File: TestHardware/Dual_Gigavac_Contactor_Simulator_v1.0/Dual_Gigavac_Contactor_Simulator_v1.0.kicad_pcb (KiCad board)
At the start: 2 copper layers, 48.1 x 35.4 mm, 69 parts, among them J1 Signal, J2 Power, J3 Contactor Driver 1, J4 Contactor Sense 2, J5 Contactor Sense 1, J6 Contactor Driver 2, Q1 Q_NMOS_DUAL_SGD, Q2 Q_NMOS_DUAL_SGD, Q3 Q_NMOS_DUAL_SGD, SW1 SW_Push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

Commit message: Minor tweaks
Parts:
- moved R22 0.13 mm to (137.5, 104.8)
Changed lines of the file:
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@@
   )
   (module Resistor_SMD:R_0603_1608Metric_Pad1.05x0.95mm_HandSolder (layer B.Cu)
-    (at 137.525 104.675)
+    (at 137.5 104.8)
     (descr "Resistor SMD 0603 (1608 Metric), square (rectangular) end terminal, IPC_7351 nominal with elongated pad for handsoldering. (Body size source: http://www.tortai-tech.com/upload/download/2011102023233369053.pdf), generated with kicad-footprint-generator")
     (tags "resistor handsolder")
@@
   (segment (start 120.25 112) (end 120.55 112.3) (width 0.2) (layer B.Cu) (net 25))
   (segment (start 121.025 112.775) (end 120.55 112.3) (width 0.2) (layer B.Cu) (net 25))
-  (via (at 120.125 104.3) (size 0.7) (drill 0.3) (layers F.Cu B.Cu) (net 26))
-  (segment (start 120.125 105.5) (end 120.125 104.3) (width 0.2) (layer B.Cu) (net 26))
-  (segment (start 120.125 104.3) (end 120.125 105.5) (width 0.2) (layer F.Cu) (net 26))
+  (segment (start 120.125 104.319254) (end 120.13569 104.308564) (width 0.2) (layer B.Cu) (net 26))
+  (segment (start 120.125 105.5) (end 120.125 104.319254) (width 0.2) (layer F.Cu) (net 26))
+  (segment (start 120.125 105.5) (end 120.125 104.319254) (width 0.2) (layer B.Cu) (net 26))
+  (segment (start 120.125 104.319254) (end 120.13569 104.308564) (width 0.2) (layer F.Cu) (net 26))
+  (via (at 120.13569 104.308564) (size 0.7) (drill 0.3) (layers F.Cu B.Cu) (net 26))
   (via (at 127.275 104.225) (size 0.7) (drill 0.3) (layers F.Cu B.Cu) (net 27))
   (segment (start 127.275 105.5) (end 127.275 104.225) (width 0.2) (layer B.Cu) (net 27))
@@
   (segment (start 130.025 114.575) (end 130.374999 114.225001) (width 0.2) (layer B.Cu) (net 37))
   (segment (start 130.374999 114.225001) (end 130.749999 114.225001) (width 0.2) (layer B.Cu) (net 37))
-  (segment (start 133.975 111.8) (end 132.9 111.8) (width 0.2) (layer F.Cu) (net 37))
-  (segment (start 135.8 109.975) (end 133.975 111.8) (width 0.2) (layer F.Cu) (net 37))
-  (segment (start 135.8 109.26) (end 135.8 109.975) (width 0.2) (layer F.Cu) (net 37))
+  (segment (start 133.025 111.8) (end 132.9 111.8) (width 0.2) (layer F.Cu) (net 37))
+  (segment (start 133.05 111.825) (end 133.025 111.8) (width 0.2) (layer F.Cu) (net 37))
+  (segment (start 133.235 111.825) (end 133.05 111.825) (width 0.2) (layer F.Cu) (net 37))
   (segment (start 138.4 107.86) (end 137.2 107.86) (width 0.2) (layer F.Cu) (net 37))
-  (segment (start 137.2 107.86) (end 135.8 109.26) (width 0.2) (layer F.Cu) (net 37))
+  (segment (start 137.2 107.86) (end 133.235 111.825) (width 0.2) (layer F.Cu) (net 37))
   (segment (start 122.45 110.675) (end 122.475 110.65) (width 0.2) (layer B.Cu) (net 38))
   (segment (start 122.45 113.425) (end 122.45 110.675) (width 0.2) (layer B.Cu) (net 38))
@@
   (segment (start 120.575 109.35) (end 121.1 109.35) (width 0.2) (layer B.Cu) (net 38))
   (segment (start 121.1 109.35) (end 121.3 109.55) (width 0.2) (layer B.Cu) (net 38))
-  (segment (start 120 100) (end 120 103.15) (width 0.2) (layer F.Cu) (net 38))
-  (segment (start 118.799999 104.725001) (end 118.05 105.475) (width 0.2) (layer F.Cu) (net 38))
-  (segment (start 118.799999 104.350001) (end 118.799999 104.725001) (width 0.2) (layer F.Cu) (net 38))
-  (segment (start 120 103.15) (end 118.799999 104.350001) (width 0.2) (layer F.Cu) (net 38))
+  (segment (start 120 103.525) (end 118.05 105.475) (width 0.2) (layer F.Cu) (net 38))
+  (segment (start 120 100) (end 120 103.525) (width 0.2) (layer F.Cu) (net 38))
   (zone (net 10) (net_name +3V3) (layer F.Cu) (hatch edge 0.508)
     (connect_pads (clearance 0.508))

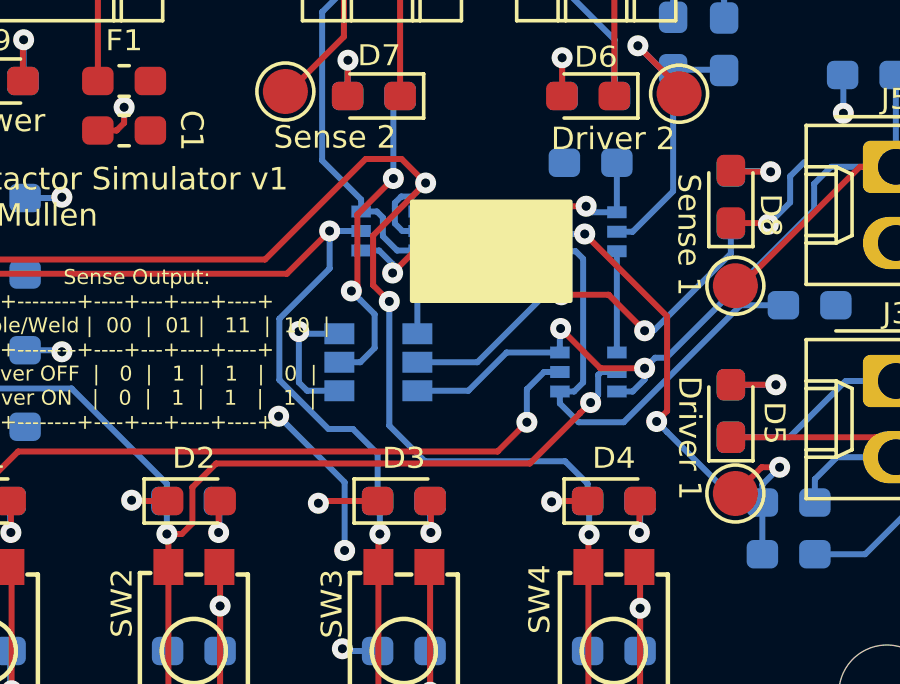
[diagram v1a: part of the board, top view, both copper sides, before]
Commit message: Fix U1A & B Orientation
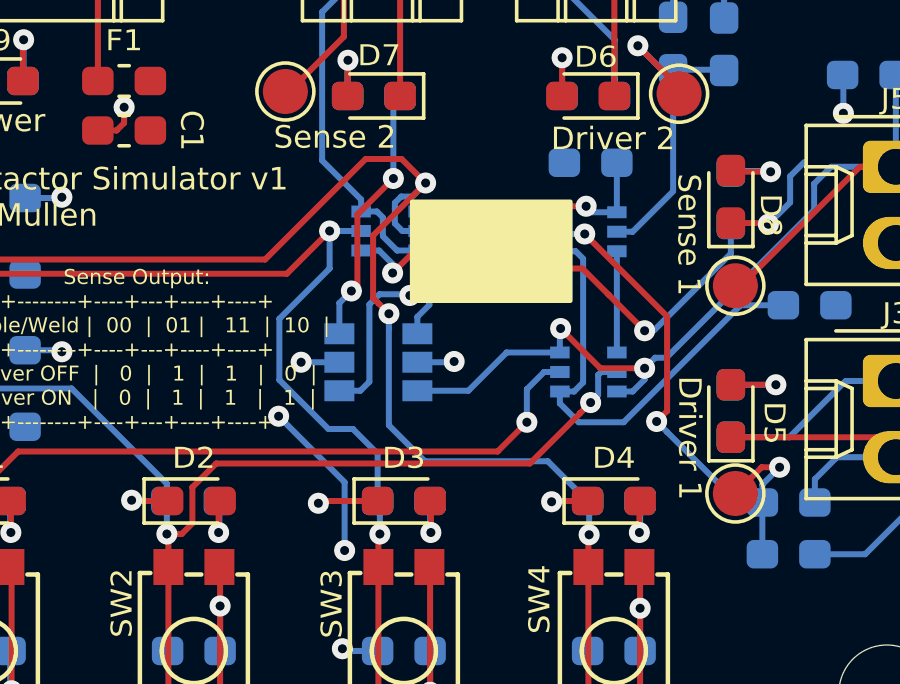
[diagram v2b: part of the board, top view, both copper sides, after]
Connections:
- U1 pad 2: Net-(R26-Pad1) -> +3V3
- U1 pad 4: +3V3 -> Net-(R26-Pad1)
- U1 pad 5: Net-(R25-Pad1) -> +3V3
- U1 pad 6: +3V3 -> Net-(R25-Pad1)
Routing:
- net Net-(R26-Pad1): track 13.9 -> 19.2 mm
- net +3V3: track 19.0 -> 17.0 mm, vias 10 -> 11
- net Net-(R25-Pad1): track 10.8 -> 8.76 mm
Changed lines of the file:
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@@
     (thickness 1.6)
     (drawings 26)
-    (tracks 391)
+    (tracks 396)
     (zones 0)
     (modules 69)
@@
     )
     (pad 5 smd rect (at 1.3 0 180) (size 1 0.7) (layers B.Cu B.Paste B.Mask)
-      (net 25 "Net-(R25-Pad1)"))
-    (pad 6 smd rect (at 1.3 0.95 180) (size 1 0.7) (layers B.Cu B.Paste B.Mask)
       (net 10 +3V3))
+    (pad 6 smd rect (at 1.3 0.95 180) (size 1 0.7) (layers B.Cu B.Paste B.Mask)
+      (net 25 "Net-(R25-Pad1)"))
     (pad 4 smd rect (at 1.3 -0.95 180) (size 1 0.7) (layers B.Cu B.Paste B.Mask)
-      (net 10 +3V3))
+      (net 24 "Net-(R26-Pad1)"))
     (pad 3 smd rect (at -1.3 -0.95 180) (size 1 0.7) (layers B.Cu B.Paste B.Mask)
       (net 37 /Sense1_Out))
     (pad 2 smd rect (at -1.3 0 180) (size 1 0.7) (layers B.Cu B.Paste B.Mask)
-      (net 24 "Net-(R26-Pad1)"))
+      (net 10 +3V3))
     (pad 1 smd rect (at -1.3 0.95 180) (size 1 0.7) (layers B.Cu B.Paste B.Mask)
       (net 38 /Sense2_Out))
@@
   (segment (start 122.725 108.4) (end 121.924999 107.599999) (width 0.2) (layer F.Cu) (net 1))
   (segment (start 121.924999 107.599999) (end 120.725001 107.599999) (width 0.2) (layer F.Cu) (net 1))
-  (segment (start 128.125 118.425) (end 127.375 117.675) (width 0.2) (layer B.Cu) (net 1))
-  (segment (start 128.125 119) (end 128.125 118.425) (width 0.2) (layer B.Cu) (net 1))
-  (segment (start 127.375 117.675) (end 122.7 117.675) (width 0.2) (layer B.Cu) (net 1))
-  (via (at 121.514175 112.346972) (size 0.7) (drill 0.3) (layers F.Cu B.Cu) (net 1))
-  (segment (start 122.7 117.675) (end 121.514175 116.489175) (width 0.2) (layer B.Cu) (net 1))
-  (segment (start 121.514175 116.489175) (end 121.514175 112.346972) (width 0.2) (layer B.Cu) (net 1))
-  (segment (start 122.375001 108.749999) (end 122.725 108.4) (width 0.2) (layer F.Cu) (net 1))
-  (segment (start 120.974999 110.150001) (end 122.375001 108.749999) (width 0.2) (layer F.Cu) (net 1))
-  (segment (start 120.974999 111.807796) (end 120.974999 110.150001) (width 0.2) (layer F.Cu) (net 1))
-  (segment (start 121.514175 112.346972) (end 120.974999 111.807796) (width 0.2) (layer F.Cu) (net 1))
   (segment (start 128.15 128.85) (end 128 129) (width 0.2) (layer F.Cu) (net 1))
   (segment (start 128.15 126.8) (end 128.15 128.85) (width 0.2) (layer F.Cu) (net 1))
+  (via (at 121.500656 112.757816) (size 0.7) (drill 0.3) (layers F.Cu B.Cu) (net 1))
+  (segment (start 128.125 119) (end 126.8 117.675) (width 0.2) (layer B.Cu) (net 1))
+  (segment (start 126.8 117.675) (end 122.7 117.675) (width 0.2) (layer B.Cu) (net 1))
+  (segment (start 120.974999 110.150001) (end 120.974999 112.232159) (width 0.2) (layer F.Cu) (net 1))
+  (segment (start 120.974999 112.232159) (end 121.150657 112.407817) (width 0.2) (layer F.Cu) (net 1))
+  (segment (start 121.500656 113.25279) (end 121.500656 112.757816) (width 0.2) (layer B.Cu) (net 1))
+  (segment (start 121.500656 116.475656) (end 121.500656 113.25279) (width 0.2) (layer B.Cu) (net 1))
+  (segment (start 122.7 117.675) (end 121.500656 116.475656) (width 0.2) (layer B.Cu) (net 1))
+  (segment (start 121.150657 112.407817) (end 121.500656 112.757816) (width 0.2) (layer F.Cu) (net 1))
+  (segment (start 122.725 108.4) (end 120.974999 110.150001) (width 0.2) (layer F.Cu) (net 1))
   (via (at 129.875 122.575) (size 0.7) (drill 0.3) (layers F.Cu B.Cu) (net 2))
   (segment (start 129.875 124) (end 129.875 122.575) (width 0.2) (layer B.Cu) (net 2))
@@
   (segment (start 116.675 101.75) (end 118.1 101.75) (width 0.2) (layer B.Cu) (net 10))
   (segment (start 118.1 101.75) (end 118.15 101.8) (width 0.2) (layer B.Cu) (net 10))
-  (segment (start 119.85 115.325) (end 118.775 115.325) (width 0.2) (layer B.Cu) (net 10))
-  (segment (start 118.775 115.325) (end 118.5 115.05) (width 0.2) (layer B.Cu) (net 10))
-  (via (at 118.5 113.35) (size 0.7) (drill 0.3) (layers F.Cu B.Cu) (net 10))
-  (segment (start 118.5 115.05) (end 118.5 113.35) (width 0.2) (layer B.Cu) (net 10))
-  (segment (start 118.575 113.425) (end 118.5 113.35) (width 0.2) (layer B.Cu) (net 10))
-  (segment (start 119.85 113.425) (end 118.575 113.425) (width 0.2) (layer B.Cu) (net 10))
   (via (at 119.95 123.925) (size 0.7) (drill 0.3) (layers F.Cu B.Cu) (net 10))
   (segment (start 121.125 124) (end 120.025 124) (width 0.2) (layer B.Cu) (net 10))
@@
   (segment (start 117.825 116.175) (end 120.025 118.375) (width 0.2) (layer B.Cu) (net 10))
   (segment (start 120.025 118.375) (end 120.025 120.65) (width 0.2) (layer B.Cu) (net 10))
+  (via (at 123.675 114.35) (size 0.7) (drill 0.3) (layers F.Cu B.Cu) (net 10))
+  (segment (start 122.45 114.375) (end 123.65 114.375) (width 0.2) (layer B.Cu) (net 10))
+  (segment (start 123.65 114.375) (end 123.675 114.35) (width 0.2) (layer B.Cu) (net 10))
+  (via (at 118.575 114.375) (size 0.7) (drill 0.3) (layers F.Cu B.Cu) (net 10))
+  (segment (start 119.85 114.375) (end 118.575 114.375) (width 0.2) (layer B.Cu) (net 10))
   (segment (start 107.5 104.95) (end 107.55 105) (width 0.2) (layer F.Cu) (net 11))
   (segment (start 107.5 100) (end 107.5 104.95) (width 0.2) (layer F.Cu) (net 11))
@@
   (segment (start 132.94 108.025) (end 132.9 107.985) (width 0.2) (layer F.Cu) (net 23))
   (segment (start 134.225 108.025) (end 132.94 108.025) (width 0.2) (layer F.Cu) (net 23))
-  (segment (start 122.45 114.375) (end 124.45 114.375) (width 0.2) (layer B.Cu) (net 24))
-  (segment (start 124.45 114.375) (end 126.7 112.125) (width 0.2) (layer B.Cu) (net 24))
-  (via (at 127.25 112.125) (size 0.7) (drill 0.3) (layers F.Cu B.Cu) (net 24))
-  (segment (start 126.7 112.125) (end 127.25 112.125) (width 0.2) (layer B.Cu) (net 24))
   (via (at 130.025 113.325) (size 0.7) (drill 0.3) (layers F.Cu B.Cu) (net 24))
-  (segment (start 127.25 112.125) (end 128.825 112.125) (width 0.2) (layer F.Cu) (net 24))
-  (segment (start 128.825 112.125) (end 130.025 113.325) (width 0.2) (layer F.Cu) (net 24))
   (segment (start 132.9 110.75) (end 132.9 109.75) (width 0.2) (layer B.Cu) (net 24))
   (segment (start 130.35 113.3) (end 132.9 110.75) (width 0.2) (layer B.Cu) (net 24))
   (segment (start 130.025 113.325) (end 130.05 113.3) (width 0.2) (layer B.Cu) (net 24))
   (segment (start 130.05 113.3) (end 130.35 113.3) (width 0.2) (layer B.Cu) (net 24))
+  (via (at 122.2 112.15) (size 0.7) (drill 0.3) (layers F.Cu B.Cu) (net 24))
+  (segment (start 128.825 112.125) (end 130.025 113.325) (width 0.2) (layer F.Cu) (net 24))
+  (segment (start 127.95 111.25) (end 128.825 112.125) (width 0.2) (layer F.Cu) (net 24))
+  (segment (start 122.2 112.15) (end 123.1 111.25) (width 0.2) (layer F.Cu) (net 24))
+  (segment (start 123.1 111.25) (end 127.95 111.25) (width 0.2) (layer F.Cu) (net 24))
+  (segment (start 122.157815 112.107815) (end 122.2 112.15) (width 0.2) (layer B.Cu) (net 24))
+  (segment (start 121.188655 112.107815) (end 122.157815 112.107815) (width 0.2) (layer B.Cu) (net 24))
+  (segment (start 120.850655 112.445815) (end 121.188655 112.107815) (width 0.2) (layer B.Cu) (net 24))
+  (segment (start 120.850655 115.024345) (end 120.850655 112.445815) (width 0.2) (layer B.Cu) (net 24))
+  (segment (start 119.85 115.325) (end 120.55 115.325) (width 0.2) (layer B.Cu) (net 24))
+  (segment (start 120.55 115.325) (end 120.850655 115.024345) (width 0.2) (layer B.Cu) (net 24))
   (via (at 121.65 108.25) (size 0.7) (drill 0.3) (layers F.Cu B.Cu) (net 25))
   (segment (start 120.45 109.45) (end 121.65 108.25) (width 0.2) (layer F.Cu) (net 25))
   (segment (start 121.65 105.725) (end 121.875 105.5) (width 0.2) (layer B.Cu) (net 25))
   (segment (start 121.65 108.25) (end 121.65 105.725) (width 0.2) (layer B.Cu) (net 25))
-  (segment (start 120.55 114.375) (end 121.025 113.9) (width 0.2) (layer B.Cu) (net 25))
-  (segment (start 119.85 114.375) (end 120.55 114.375) (width 0.2) (layer B.Cu) (net 25))
-  (segment (start 121.025 113.9) (end 121.025 112.775) (width 0.2) (layer B.Cu) (net 25))
   (via (at 120.25 112) (size 0.7) (drill 0.3) (layers F.Cu B.Cu) (net 25))
   (segment (start 120.45 109.45) (end 120.45 111.8) (width 0.2) (layer F.Cu) (net 25))
   (segment (start 120.45 111.8) (end 120.25 112) (width 0.2) (layer F.Cu) (net 25))
-  (segment (start 120.25 112) (end 120.55 112.3) (width 0.2) (layer B.Cu) (net 25))
-  (segment (start 121.025 112.775) (end 120.55 112.3) (width 0.2) (layer B.Cu) (net 25))
+  (segment (start 119.85 112.4) (end 120.25 112) (width 0.2) (layer B.Cu) (net 25))
+  (segment (start 119.85 113.425) (end 119.85 112.4) (width 0.2) (layer B.Cu) (net 25))
   (segment (start 120.125 104.319254) (end 120.13569 104.308564) (width 0.2) (layer B.Cu) (net 26))
   (segment (start 120.125 105.5) (end 120.125 104.319254) (width 0.2) (layer F.Cu) (net 26))
@@
   (segment (start 137.2 107.86) (end 133.235 111.825) (width 0.2) (layer F.Cu) (net 37))
   (segment (start 122.45 110.675) (end 122.475 110.65) (width 0.2) (layer B.Cu) (net 38))
-  (segment (start 122.45 113.425) (end 122.45 110.675) (width 0.2) (layer B.Cu) (net 38))
   (segment (start 119.03 100) (end 116.675 100) (width 0.2) (layer B.Cu) (net 38))
   (segment (start 120 100) (end 119.03 100) (width 0.2) (layer B.Cu) (net 38))
@@
   (segment (start 120 103.525) (end 118.05 105.475) (width 0.2) (layer F.Cu) (net 38))
   (segment (start 120 100) (end 120 103.525) (width 0.2) (layer F.Cu) (net 38))
+  (segment (start 122.850001 112.462001) (end 122.850001 111.800001) (width 0.2) (layer B.Cu) (net 38))
+  (segment (start 122.45 113.425) (end 122.45 112.862002) (width 0.2) (layer B.Cu) (net 38))
+  (segment (start 122.45 112.862002) (end 122.850001 112.462001) (width 0.2) (layer B.Cu) (net 38))
+  (segment (start 122.475 111.425) (end 122.475 110.65) (width 0.2) (layer B.Cu) (net 38))
+  (segment (start 122.850001 111.800001) (end 122.475 111.425) (width 0.2) (layer B.Cu) (net 38))
   (zone (net 10) (net_name +3V3) (layer F.Cu) (hatch edge 0.508)
     (connect_pads (clearance 0.508))
